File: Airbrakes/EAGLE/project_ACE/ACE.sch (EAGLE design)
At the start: 7 parts, among them J2 SMD, J3 PTH, J4 SMD

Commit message: Fix version
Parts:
- added U$1: MIKROE-ALTITUDE-6-CLICK-DVC, MIKROE-4903:MIKROE-ALTITUDE-6-CLICK-DVC
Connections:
- removed net SCL/SCK/RX: JP1.4
- removed net SDA/MISO/TX: JP1.5
- net GND: now also U$1.GND_0, U$1.GND_1
- net SCL: now also JP1.4, U$1.SCL
- net SDA: now also JP1.5, U$1.SDA
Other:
- note added: "Altitude 6 Click Pinout"
- moved on the sheet: J2, J3, J4, J6, JP1, JP2

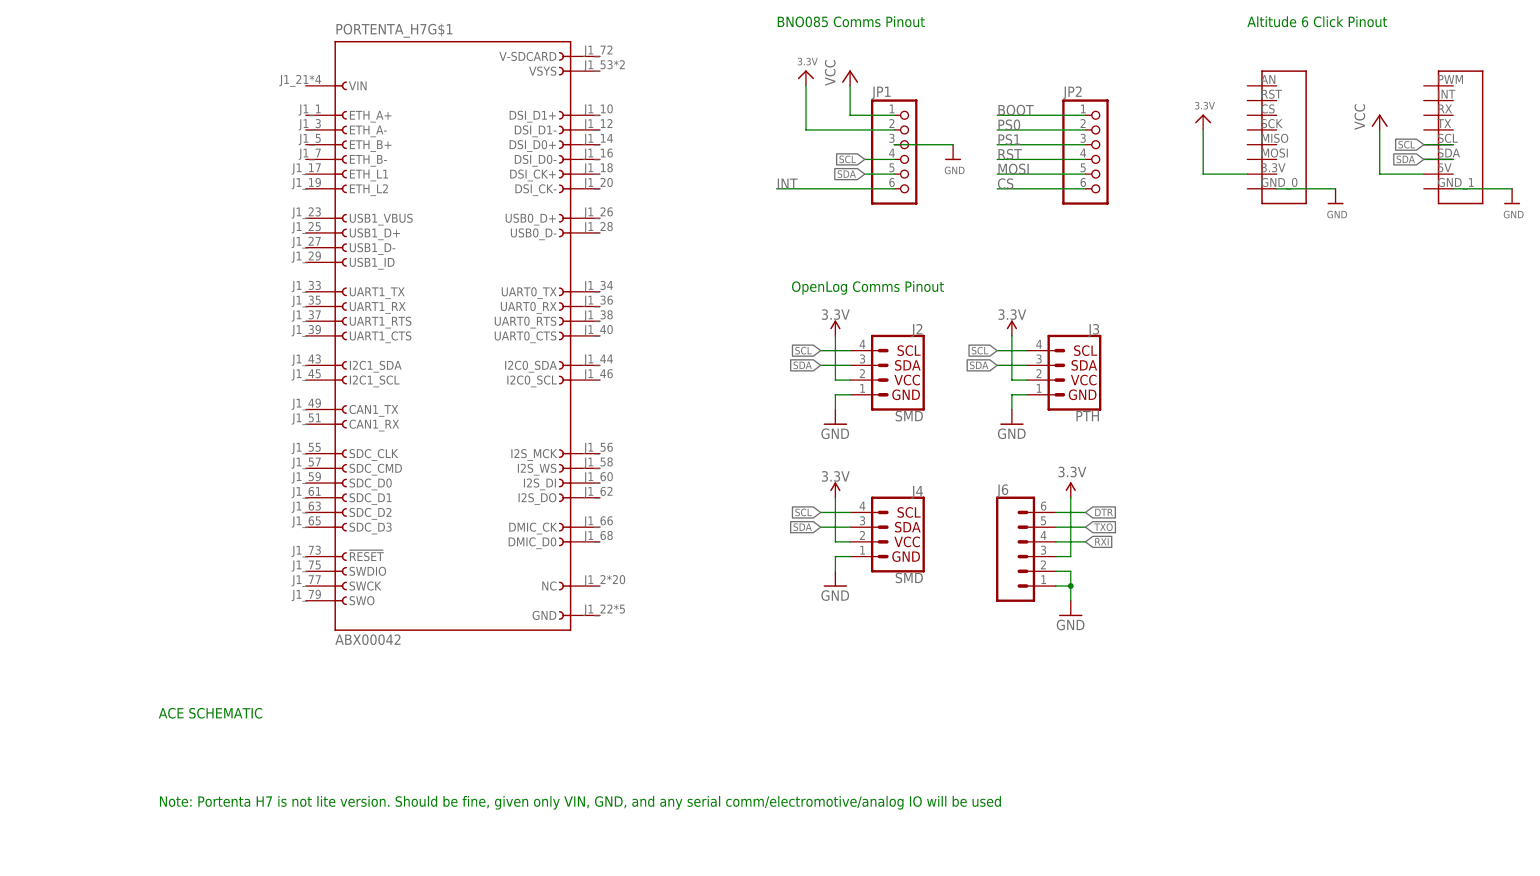
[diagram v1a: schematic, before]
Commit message: Update CAD with BNO08x footprint
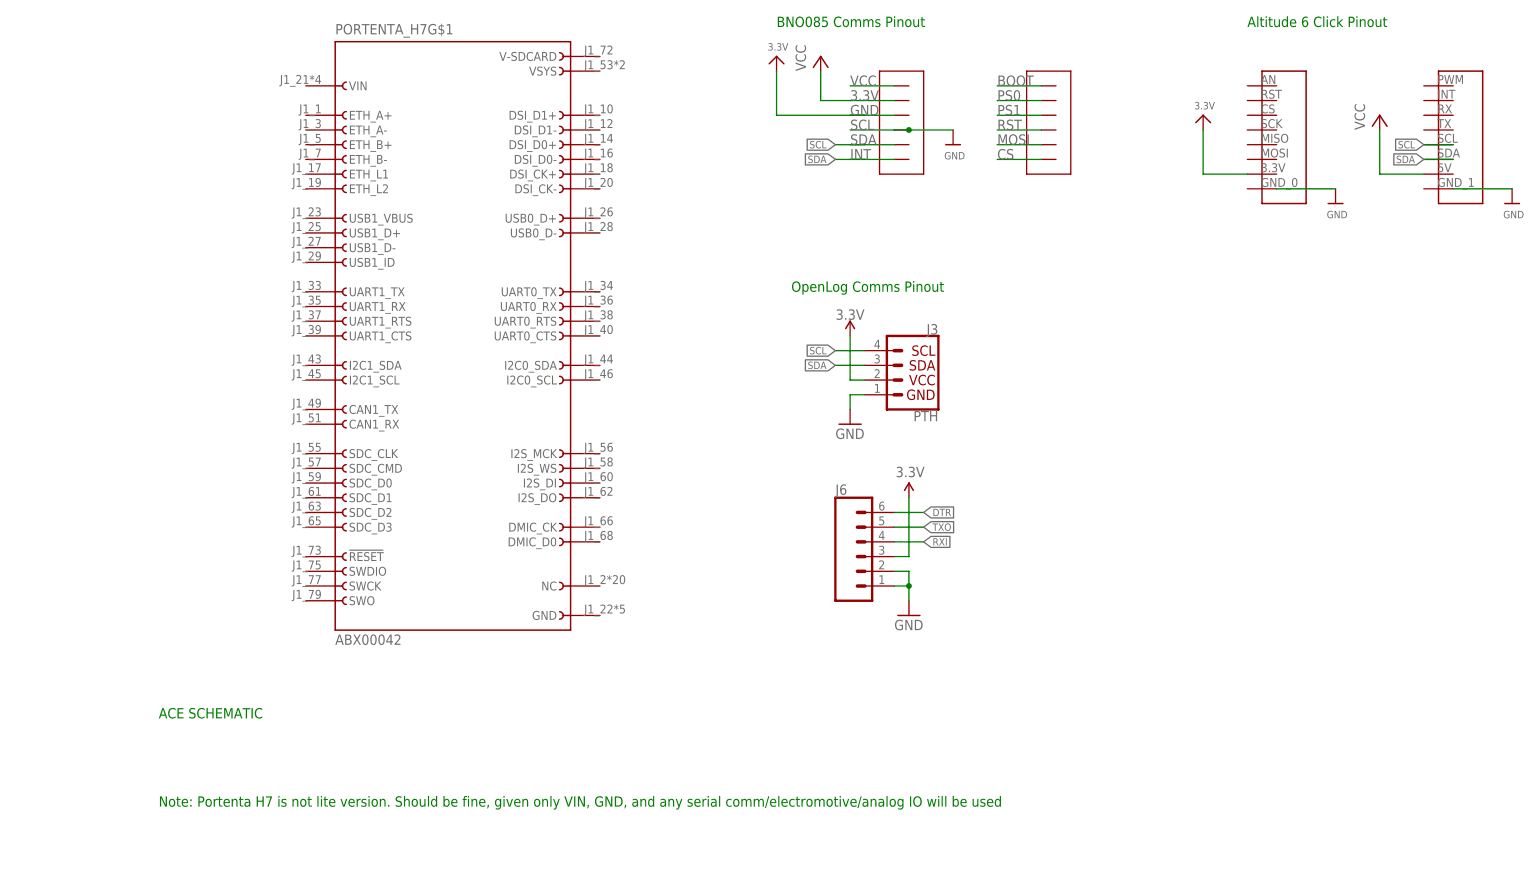
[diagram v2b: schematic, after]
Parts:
- removed J2, J4: SMD, SparkFun-Connectors:QWIIC_CONNECTORJS-1MM
- removed JP1, JP2: (no value), microbuilder:HEADER-1X670MIL
- added U$5: ADAFRUIT_BNO08X, ADAFRUIT_BNO08x:ADAFRUIT_BNO08X
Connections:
- removed net BOOT: JP2.1
- removed net CS: JP2.6
- removed net INT: JP1.6
- removed net MOSI: JP2.5
- removed net PS0: JP2.2
- removed net PS1: JP2.3
- removed net RST: JP2.4
- removed net VCC: JP1.1
- new net N$1: U$1.GND_1
- net 3.3V: no longer J2.2, J4.2, JP1.2
- net GND: now also U$5.SCL; no longer J2.1, J4.1, JP1.3, U$1.GND_1
- net SCL: no longer J2.4, J4.4, JP1.4
- net SDA: no longer J2.3, J4.3, JP1.5
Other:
- moved on the sheet: J3, J6

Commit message: Reorganize board layout and fix nets
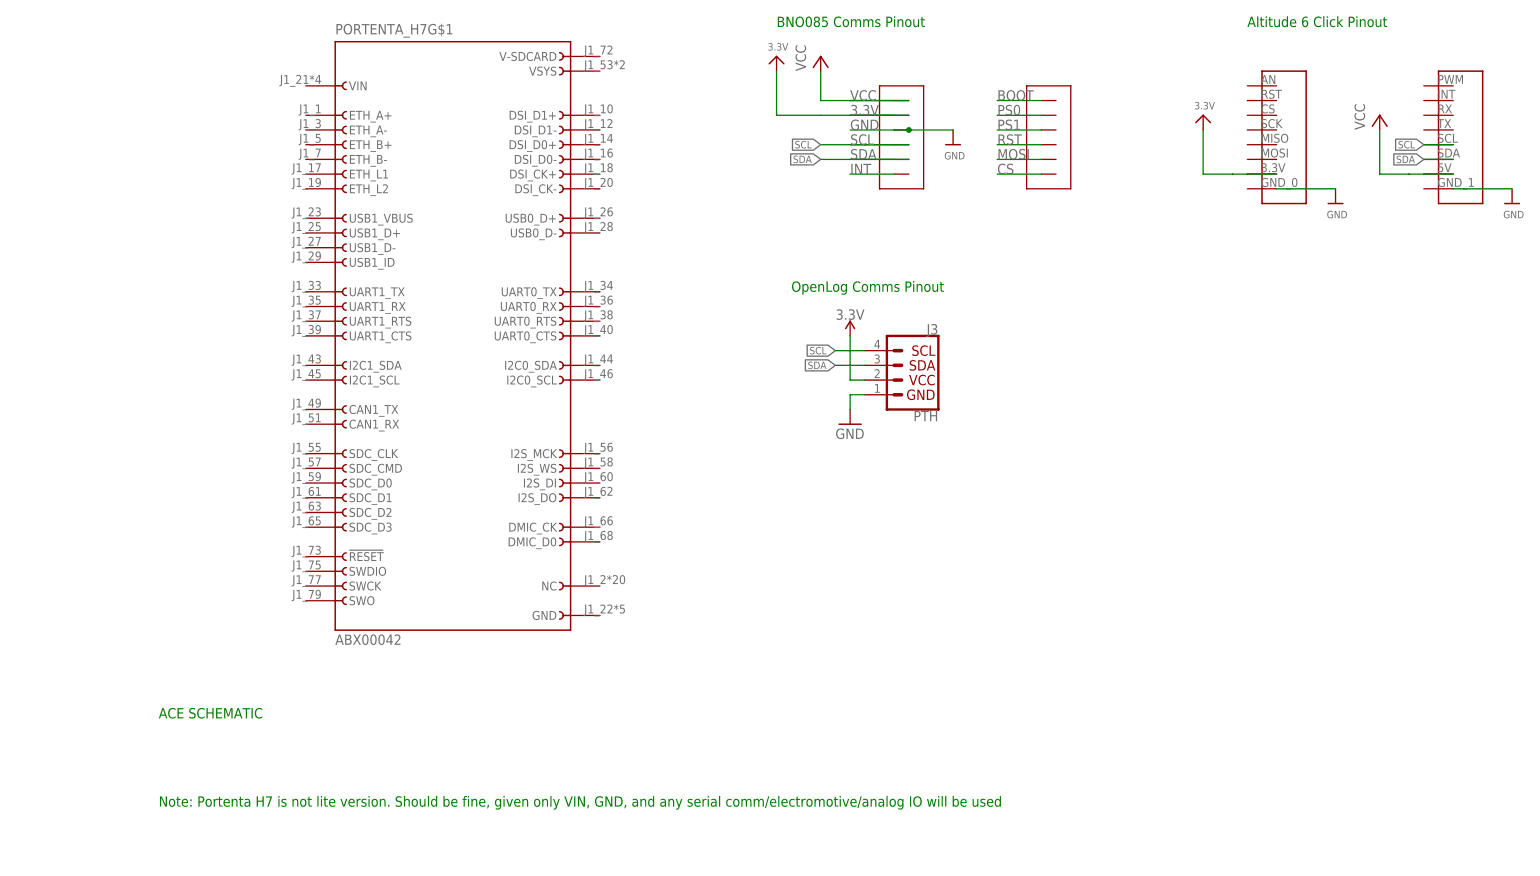
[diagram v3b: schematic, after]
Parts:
- removed J6: (no value), SparkFun-Connectors:CONN_06NO_SILK_NO_POP
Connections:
- removed net DTR: J6.6
- removed net RXI: J6.4
- removed net TXO: J6.5
- new net VCC: U$1.5V, U$5.VCC
- net 3.3V: now also U$1.3.3V, U$5.3.3V; no longer J6.3
- net GND: now also U$5.GND; no longer J6.1, J6.2, U$5.SCL
- net SCL: now also U$5.SCL
- net SDA: now also U$5.SDA
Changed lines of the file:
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@@
 <parts>
 <part name="PORTENTA_H7" library="ABX00042" deviceset="ABX00042" device=""/>
-<part name="GND6" library="SparkFun" deviceset="GND" device=""/>
 <part name="SUPPLY7" library="SparkFun-PowerSymbols" deviceset="3.3V" device=""/>
 <part name="J3" library="SparkX" deviceset="I2C_STANDARD" device="_NO_SILK" value="PTH"/>
 <part name="GND12" library="SparkFun" deviceset="GND" device=""/>
-<part name="P+1" library="SparkFun" deviceset="3.3V" device=""/>
-<part name="J6" library="SparkFun-Connectors" deviceset="CONN_06" device="NO_SILK_NO_POP"/>
 <part name="U$2" library="microbuilder" deviceset="GND" device=""/>
 <part name="U$3" library="microbuilder" deviceset="GND" device=""/>
@@
 <attribute name="VALUE" x="30.48" y="17.78" size="1.778" layer="96"/>
 </instance>
-<instance part="GND6" gate="1" x="129.54" y="22.86" smashed="yes">
-<attribute name="VALUE" x="127" y="20.32" size="1.778" layer="96"/>
-</instance>
 <instance part="SUPPLY7" gate="G$1" x="119.38" y="71.12" smashed="yes">
 <attribute name="VALUE" x="119.38" y="73.914" size="1.778" layer="96" align="bottom-center"/>
@@
 <instance part="GND12" gate="1" x="119.38" y="55.88" smashed="yes">
 <attribute name="VALUE" x="116.84" y="53.34" size="1.778" layer="96"/>
-</instance>
-<instance part="P+1" gate="G$1" x="129.54" y="43.18" smashed="yes">
-<attribute name="VALUE" x="127.254" y="46.736" size="1.778" layer="96"/>
-</instance>
-<instance part="J6" gate="G$1" x="121.92" y="33.02" smashed="yes">
-<attribute name="VALUE" x="116.84" y="23.114" size="1.778" layer="96" font="vector"/>
-<attribute name="NAME" x="116.84" y="43.688" size="1.778" layer="95" font="vector"/>
 </instance>
 <instance part="U$2" gate="G$1" x="203.2" y="93.98" smashed="yes">
@@
 <attribute name="VALUE" x="135.636" y="101.6" size="1.27" layer="96"/>
 </instance>
-<instance part="U$5" gate="G$1" x="121.92" y="99.06" smashed="yes"/>
+<instance part="U$5" gate="G$1" x="121.92" y="96.52" smashed="yes"/>
 </instances>
 <busses>
@@
 <nets>
 <net name="GND" class="2">
-<segment>
-<wire x1="129.54" y1="27.94" x2="129.54" y2="25.4" width="0.1524" layer="91"/>
-<pinref part="GND6" gate="1" pin="GND"/>
-<wire x1="127" y1="30.48" x2="129.54" y2="30.48" width="0.1524" layer="91"/>
-<wire x1="129.54" y1="30.48" x2="129.54" y2="27.94" width="0.1524" layer="91"/>
-<wire x1="127" y1="27.94" x2="129.54" y2="27.94" width="0.1524" layer="91"/>
-<junction x="129.54" y="27.94"/>
-<pinref part="J6" gate="G$1" pin="1"/>
-<pinref part="J6" gate="G$1" pin="2"/>
-</segment>
 <segment>
 <pinref part="J3" gate="G$1" pin="GND"/>
@@
 <segment>
 <pinref part="U$2" gate="G$1" pin="GND"/>
+<pinref part="U$1" gate="G$1" pin="GND_0"/>
 <wire x1="193.04" y1="96.52" x2="203.2" y2="96.52" width="0.1524" layer="91"/>
-<pinref part="U$1" gate="G$1" pin="GND_0"/>
 </segment>
 <segment>
 <pinref part="U$7" gate="G$1" pin="GND"/>
 <wire x1="127" y1="106.68" x2="129.54" y2="106.68" width="0.1524" layer="91"/>
-<pinref part="U$5" gate="G$1" pin="SCL"/>
+<pinref part="U$5" gate="G$1" pin="GND"/>
 <wire x1="129.54" y1="106.68" x2="137.16" y2="106.68" width="0.1524" layer="91"/>
 <junction x="129.54" y="106.68"/>
@@
 <net name="VCC" class="2">
 <segment>
-<wire x1="218.44" y1="99.06" x2="210.82" y2="99.06" width="0.1524" layer="91"/>
+<wire x1="218.44" y1="99.06" x2="215.9" y2="99.06" width="0.1524" layer="91"/>
+<wire x1="215.9" y1="99.06" x2="210.82" y2="99.06" width="0.1524" layer="91"/>
 <wire x1="210.82" y1="99.06" x2="210.82" y2="106.68" width="0.1524" layer="91"/>
 <pinref part="P+2" gate="VCC" pin="VCC"/>
+<pinref part="U$1" gate="G$1" pin="5V"/>
+<wire x1="223.52" y1="99.06" x2="218.44" y2="99.06" width="0.1524" layer="91"/>
 </segment>
 <segment>
@@
 <wire x1="114.3" y1="111.76" x2="114.3" y2="116.84" width="0.1524" layer="91"/>
 <pinref part="P+3" gate="VCC" pin="VCC"/>
+<pinref part="U$5" gate="G$1" pin="VCC"/>
+<wire x1="129.54" y1="111.76" x2="119.38" y2="111.76" width="0.1524" layer="91"/>
 </segment>
 </net>
@@
 </segment>
 <segment>
-<wire x1="127" y1="33.02" x2="129.54" y2="33.02" width="0.1524" layer="91"/>
-<wire x1="129.54" y1="33.02" x2="129.54" y2="43.18" width="0.1524" layer="91"/>
-<pinref part="P+1" gate="G$1" pin="3.3V"/>
-<pinref part="J6" gate="G$1" pin="3"/>
+<wire x1="187.96" y1="99.06" x2="185.42" y2="99.06" width="0.1524" layer="91"/>
+<wire x1="185.42" y1="99.06" x2="180.34" y2="99.06" width="0.1524" layer="91"/>
+<wire x1="180.34" y1="99.06" x2="180.34" y2="106.68" width="0.1524" layer="91"/>
+<pinref part="U$4" gate="G$1" pin="3.3V"/>
+<pinref part="U$1" gate="G$1" pin="3.3V"/>
+<wire x1="193.04" y1="99.06" x2="187.96" y2="99.06" width="0.1524" layer="91"/>
 </segment>
 <segment>
-<wire x1="187.96" y1="99.06" x2="180.34" y2="99.06" width="0.1524" layer="91"/>
-<wire x1="180.34" y1="99.06" x2="180.34" y2="106.68" width="0.1524" layer="91"/>
-<pinref part="U$4" gate="G$1" pin="3.3V"/>
-</segment>
-<segment>
-<wire x1="121.92" y1="109.22" x2="106.68" y2="109.22" width="0.1524" layer="91"/>
+<wire x1="121.92" y1="109.22" x2="114.3" y2="109.22" width="0.1524" layer="91"/>
+<wire x1="114.3" y1="109.22" x2="106.68" y2="109.22" width="0.1524" layer="91"/>
 <wire x1="106.68" y1="109.22" x2="106.68" y2="116.84" width="0.1524" layer="91"/>
 <pinref part="U$6" gate="G$1" pin="3.3V"/>
-</segment>
-</net>
-<net name="TXO" class="0">
-<segment>
-<wire x1="127" y1="38.1" x2="132.08" y2="38.1" width="0.1524" layer="91"/>
-<label x="132.08" y="38.1" size="1.27" layer="95" rot="MR180" xref="yes"/>
-<pinref part="J6" gate="G$1" pin="5"/>
-</segment>
-</net>
-<net name="DTR" class="0">
-<segment>
-<wire x1="127" y1="40.64" x2="132.08" y2="40.64" width="0.1524" layer="91"/>
-<label x="132.08" y="40.64" size="1.27" layer="95" rot="MR180" xref="yes"/>
-<pinref part="J6" gate="G$1" pin="6"/>
-</segment>
-</net>
-<net name="RXI" class="0">
-<segment>
-<wire x1="127" y1="35.56" x2="132.08" y2="35.56" width="0.1524" layer="91"/>
-<label x="132.08" y="35.56" size="1.27" layer="95" rot="MR180" xref="yes"/>
-<pinref part="J6" gate="G$1" pin="4"/>
+<pinref part="U$5" gate="G$1" pin="3.3V"/>
+<wire x1="129.54" y1="109.22" x2="121.92" y2="109.22" width="0.1524" layer="91"/>
 </segment>
 </net>
@@
 </segment>
 <segment>
-<wire x1="121.92" y1="104.14" x2="116.84" y2="104.14" width="0.1524" layer="91"/>
-<label x="116.84" y="104.14" size="1.27" layer="95" rot="R180" xref="yes"/>
+<wire x1="121.92" y1="104.14" x2="114.3" y2="104.14" width="0.1524" layer="91"/>
+<label x="114.3" y="104.14" size="1.27" layer="95" rot="R180" xref="yes"/>
+<pinref part="U$5" gate="G$1" pin="SCL"/>
+<wire x1="121.92" y1="104.14" x2="129.54" y2="104.14" width="0.1524" layer="91"/>
 </segment>
 </net>
@@
 </segment>
 <segment>
-<wire x1="121.92" y1="101.6" x2="116.84" y2="101.6" width="0.1524" layer="91"/>
-<label x="116.84" y="101.6" size="1.27" layer="95" rot="R180" xref="yes"/>
+<wire x1="121.92" y1="101.6" x2="114.3" y2="101.6" width="0.1524" layer="91"/>
+<label x="114.3" y="101.6" size="1.27" layer="95" rot="R180" xref="yes"/>
+<pinref part="U$5" gate="G$1" pin="SDA"/>
+<wire x1="121.92" y1="101.6" x2="129.54" y2="101.6" width="0.1524" layer="91"/>
 </segment>
 </net>
@@
 <segment>
 <pinref part="U$3" gate="G$1" pin="GND"/>
+<pinref part="U$1" gate="G$1" pin="GND_1"/>
 <wire x1="223.52" y1="96.52" x2="233.68" y2="96.52" width="0.1524" layer="91"/>
-<pinref part="U$1" gate="G$1" pin="GND_1"/>
 </segment>
 </net>

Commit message: Update schematic and board with Portenta pin headers
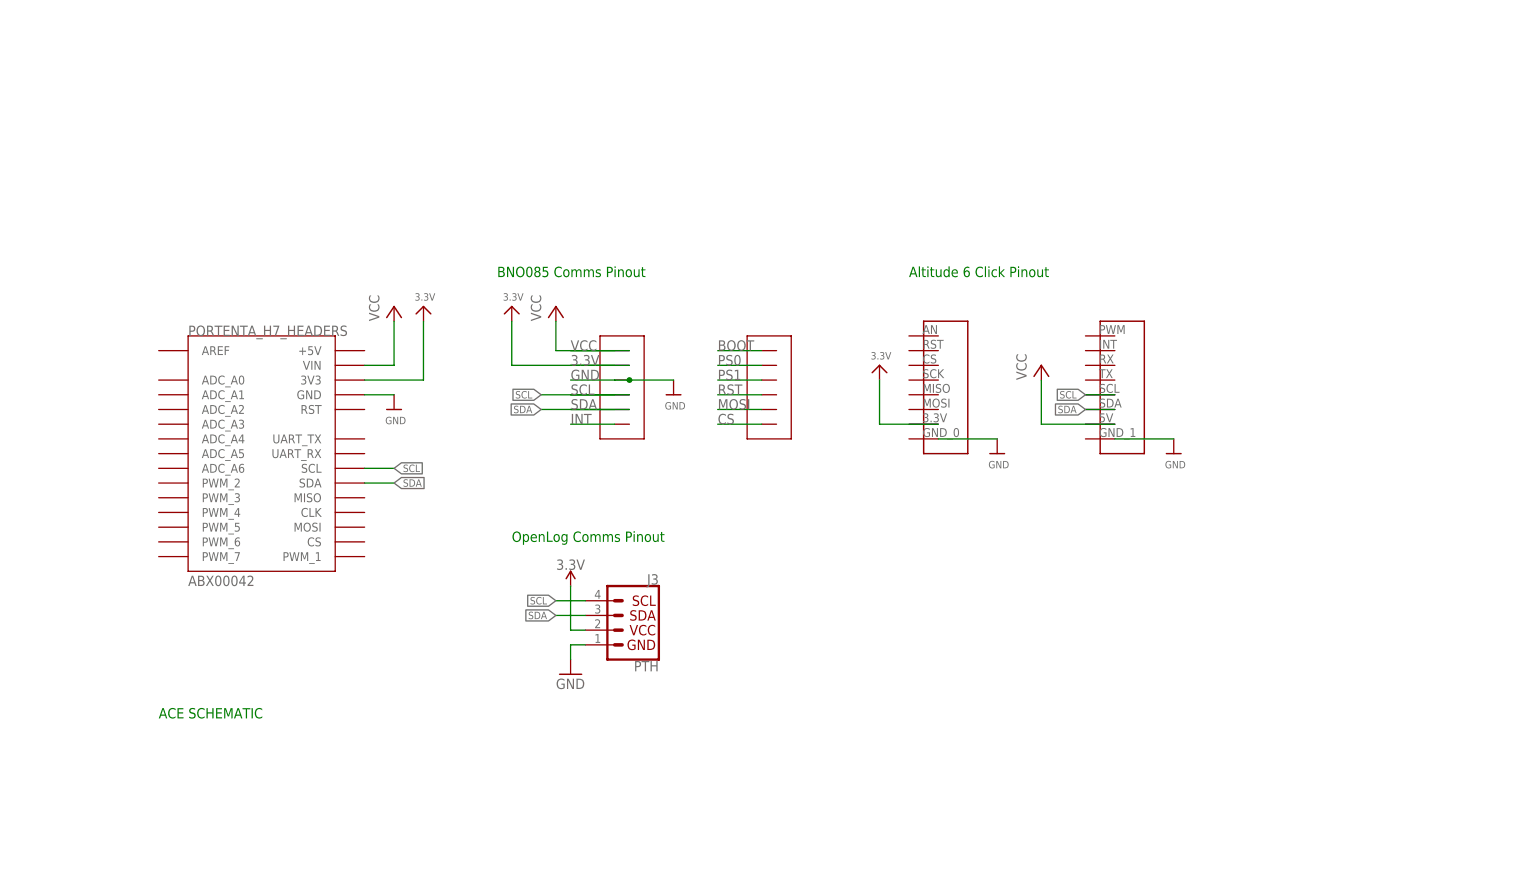
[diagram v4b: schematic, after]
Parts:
- removed PORTENTA_H7: ABX00042, ABX00042:ABX00042
- added U$10: ABX00042_HEADERS_IO, ABX00042:ABX00042_HEADERS_IO
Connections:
- net 3.3V: now also U$10.3V3
- net GND: now also U$10.GND
- net SCL: now also U$10.SCL
- net SDA: now also U$10.SDA
- net VCC: now also U$10.VIN
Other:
- note removed: "Note: Portenta H7 is not lite version. Should be fine, given only VIN, GND, and any serial comm/electromotive/analog IO will be used"
- moved on the sheet: J3
